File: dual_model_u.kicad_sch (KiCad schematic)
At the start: 6 parts, among them J1 TYPE_C_31_M_04, J2 USB_B_Micro, J3 Conn_01x04, J4 Conn_01x04

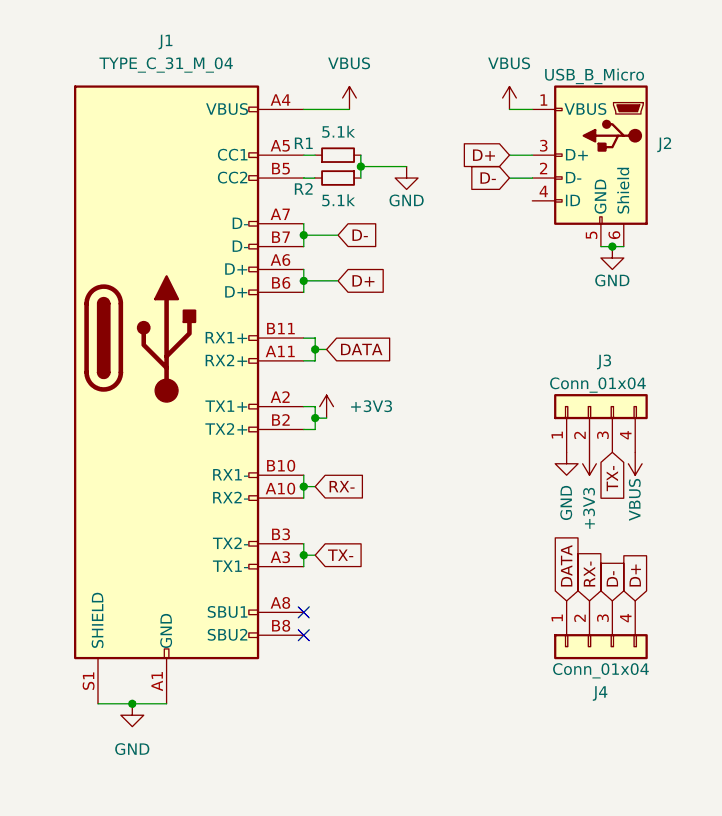
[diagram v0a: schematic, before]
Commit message: Cleaned up sheets
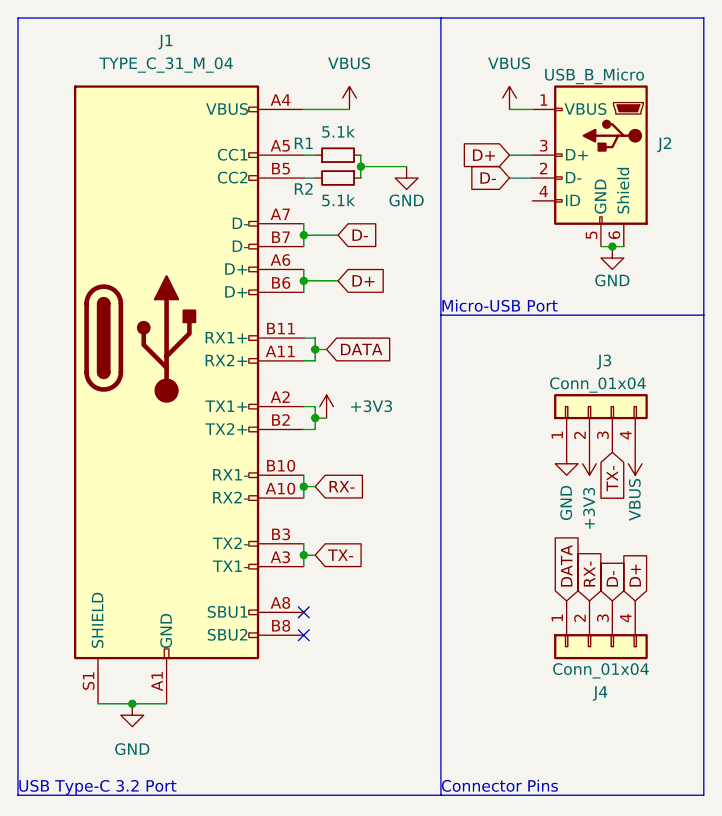
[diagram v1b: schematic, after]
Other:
- note added: "Connector Pins"
- note added: "Micro-USB Port"
- note added: "USB Type-C 3.2 Port"
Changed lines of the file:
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@@
+    (stroke (width 0) (type default) (color 0 0 0 0))
+  )
+  (polyline (pts (xy 96.52 59.69) (xy 96.52 146.05))
+    (stroke (width 0) (type default) (color 0 0 0 0))
+  )
+  (polyline (pts (xy 96.52 59.69) (xy 143.51 59.69))
+    (stroke (width 0) (type default) (color 0 0 0 0))
+  )
+  (polyline (pts (xy 143.51 146.05) (xy 96.52 146.05))
     (stroke (width 0) (type default) (color 0 0 0 0))
   )
@@
   )
   (wire (pts (xy 128.27 74.93) (xy 129.54 74.93))
+    (stroke (width 0) (type default) (color 0 0 0 0))
+  )
+  (polyline (pts (xy 172.72 146.05) (xy 143.51 146.05))
+    (stroke (width 0) (type default) (color 0 0 0 0))
+  )
+  (polyline (pts (xy 172.72 59.69) (xy 172.72 92.71))
+    (stroke (width 0) (type default) (color 0 0 0 0))
+  )
+  (polyline (pts (xy 172.72 92.71) (xy 172.72 146.05))
     (stroke (width 0) (type default) (color 0 0 0 0))
   )
@@
     (stroke (width 0) (type default) (color 0 0 0 0))
   )
+  (polyline (pts (xy 143.51 59.69) (xy 172.72 59.69))
+    (stroke (width 0) (type default) (color 0 0 0 0))
+  )
   (wire (pts (xy 109.22 135.89) (xy 113.03 135.89))
     (stroke (width 0) (type default) (color 0 0 0 0))
@@
     (stroke (width 0) (type default) (color 0 0 0 0))
   )
+  (polyline (pts (xy 172.72 92.71) (xy 143.51 92.71))
+    (stroke (width 0) (type default) (color 0 0 0 0))
+  )
   (wire (pts (xy 128.27 77.47) (xy 129.54 77.47))
     (stroke (width 0) (type default) (color 0 0 0 0))
@@
     (stroke (width 0) (type default) (color 0 0 0 0))
   )
+  (polyline (pts (xy 143.51 59.69) (xy 143.51 146.05))
+    (stroke (width 0) (type default) (color 0 0 0 0))
+  )
+  (text "USB Type-C 3.2 Port" (at 96.52 146.05 0)
+    (effects (font (size 1.27 1.27)) (justify left bottom))
+  )
+  (text "Connector Pins" (at 143.51 146.05 0)
+    (effects (font (size 1.27 1.27)) (justify left bottom))
+  )
+  (text "Micro-USB Port" (at 143.51 92.71 0)
+    (effects (font (size 1.27 1.27)) (justify left bottom))
+  )
   (global_label "DATA" (shape input) (at 130.81 96.52 0) (fields_autoplaced)
